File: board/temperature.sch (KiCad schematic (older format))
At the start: 3 parts, among them P201 CONN_2, U201 MAX6675

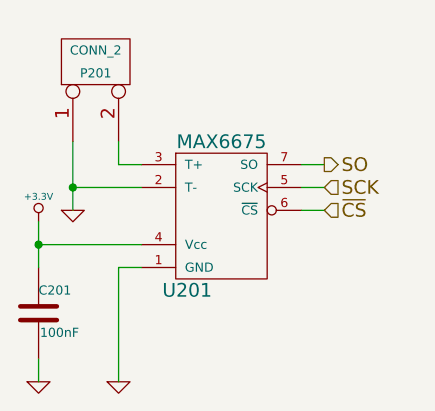
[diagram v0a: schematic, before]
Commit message: Selected Part Numbers for all Components
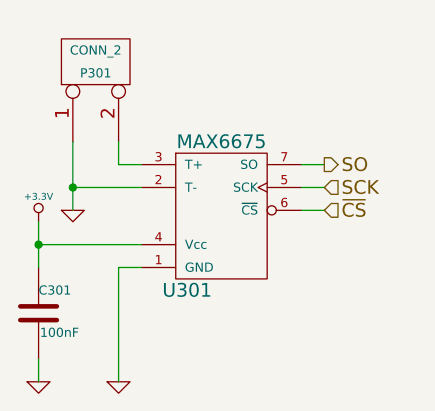
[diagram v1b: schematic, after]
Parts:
- C201: Part Number (none) -> CL10F104ZA8NNNC
- P201: Part Number (none) -> 1716020000
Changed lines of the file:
@@
 AR Path="/52EEE819/52E6B9FE" Ref="C201"  Part="1"
 AR Path="/52E79355/52E6B9FE" Ref="C301"  Part="1"
-F 0 "C201" H 4850 3900 40  0000 L CNN
+F 0 "C301" H 4850 3900 40  0000 L CNN
 F 1 "100nF" H 4856 3715 40  0000 L CNN
 F 2 "" H 4888 3650 30  0000 C CNN
 F 3 "" H 4850 3800 60  0000 C CNN
+F 4 "CL10F104ZA8NNNC" H 4850 3800 60  0001 C CNN "Part Number"
 	1    4850 3800
 	1    0    0    -1
 $EndComp
 $Comp
-L GND #PWR0116
+L GND #PWR0121
 U 1 1 52E6BA13
 P 5200 4100
-AR Path="/52EEE819/52E6BA13" Ref="#PWR0116"  Part="1"
-AR Path="/52E79355/52E6BA13" Ref="#PWR0120"  Part="1"
-F 0 "#PWR0116" H 5200 4100 30  0001 C CNN
+AR Path="/52EEE819/52E6BA13" Ref="#PWR0121"  Part="1"
+AR Path="/52E79355/52E6BA13" Ref="#PWR0125"  Part="1"
+F 0 "#PWR0125" H 5200 4100 30  0001 C CNN
 F 1 "GND" H 5200 4030 30  0001 C CNN
 F 2 "" H 5200 4100 60  0000 C CNN
@@
 	4850 3400 4850 3600
 $Comp
-L +3.3V #PWR0117
+L +3.3V #PWR0122
 U 1 1 52E6BA4F
 P 4850 3400
-AR Path="/52EEE819/52E6BA4F" Ref="#PWR0117"  Part="1"
-AR Path="/52E79355/52E6BA4F" Ref="#PWR0121"  Part="1"
-F 0 "#PWR0117" H 4850 3360 30  0001 C CNN
+AR Path="/52EEE819/52E6BA4F" Ref="#PWR0122"  Part="1"
+AR Path="/52E79355/52E6BA4F" Ref="#PWR0126"  Part="1"
+F 0 "#PWR0126" H 4850 3360 30  0001 C CNN
 F 1 "+3.3V" H 4850 3510 30  0000 C CNN
 F 2 "" H 4850 3400 60  0000 C CNN
@@
 Connection ~ 4850 3500
 $Comp
-L GND #PWR0118
+L GND #PWR0123
 U 1 1 52E6BA82
 P 4850 4100
-AR Path="/52EEE819/52E6BA82" Ref="#PWR0118"  Part="1"
-AR Path="/52E79355/52E6BA82" Ref="#PWR0122"  Part="1"
-F 0 "#PWR0118" H 4850 4100 30  0001 C CNN
+AR Path="/52EEE819/52E6BA82" Ref="#PWR0123"  Part="1"
+AR Path="/52E79355/52E6BA82" Ref="#PWR0127"  Part="1"
+F 0 "#PWR0127" H 4850 4100 30  0001 C CNN
 F 1 "GND" H 4850 4030 30  0001 C CNN
 F 2 "" H 4850 4100 60  0000 C CNN
@@
 AR Path="/52EEE819/52E6BAA9" Ref="P201"  Part="1"
 AR Path="/52E79355/52E6BAA9" Ref="P301"  Part="1"
-F 0 "P201" V 5050 2700 40  0000 C CNN
+F 0 "P301" V 5050 2700 40  0000 C CNN
 F 1 "CONN_2" V 5150 2700 40  0000 C CNN
 F 2 "" H 5100 2700 60  0000 C CNN
 F 3 "" H 5100 2700 60  0000 C CNN
+F 4 "1716020000" V 5100 2700 60  0001 C CNN "Part Number"
 	1    5100 2700
 	0    -1   -1   0
@@
 AR Path="/52EEE819/52E6BBF9" Ref="U201"  Part="1"
 AR Path="/52E79355/52E6BBF9" Ref="U301"  Part="1"
-F 0 "U201" H 5500 3100 60  0000 C CNN
+F 0 "U301" H 5500 3100 60  0000 C CNN
 F 1 "MAX6675" H 5650 3750 60  0000 C CNN
 F 2 "" H 5650 3400 60  0000 C CNN
@@
 $EndComp
 $Comp
-L GND #PWR0119
+L GND #PWR0124
 U 1 1 52E6BC15
 P 5000 3350
-AR Path="/52EEE819/52E6BC15" Ref="#PWR0119"  Part="1"
-AR Path="/52E79355/52E6BC15" Ref="#PWR0123"  Part="1"
-F 0 "#PWR0119" H 5000 3350 30  0001 C CNN
+AR Path="/52EEE819/52E6BC15" Ref="#PWR0124"  Part="1"
+AR Path="/52E79355/52E6BC15" Ref="#PWR0128"  Part="1"
+F 0 "#PWR0128" H 5000 3350 30  0001 C CNN
 F 1 "GND" H 5000 3280 30  0001 C CNN
 F 2 "" H 5000 3350 60  0000 C CNN

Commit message: Resolved issues while associating footprints.
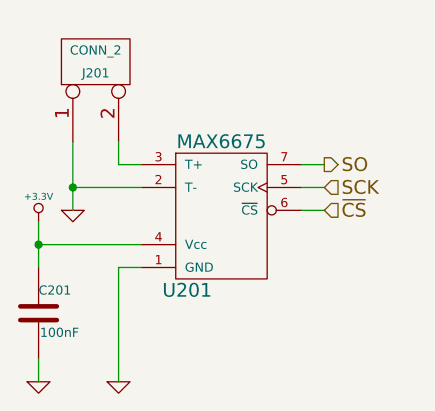
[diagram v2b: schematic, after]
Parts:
- renumbered P201 to J201
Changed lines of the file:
@@
 AR Path="/52EEE819/52E6B9FE" Ref="C201"  Part="1"
 AR Path="/52E79355/52E6B9FE" Ref="C301"  Part="1"
-F 0 "C301" H 4850 3900 40  0000 L CNN
+F 0 "C201" H 4850 3900 40  0000 L CNN
 F 1 "100nF" H 4856 3715 40  0000 L CNN
 F 2 "" H 4888 3650 30  0000 C CNN
@@
 $EndComp
 $Comp
-L GND #PWR0121
+L GND #PWR219
 U 1 1 52E6BA13
 P 5200 4100
-AR Path="/52EEE819/52E6BA13" Ref="#PWR0121"  Part="1"
-AR Path="/52E79355/52E6BA13" Ref="#PWR0125"  Part="1"
-F 0 "#PWR0125" H 5200 4100 30  0001 C CNN
+AR Path="/52EEE819/52E6BA13" Ref="#PWR219"  Part="1"
+AR Path="/52E79355/52E6BA13" Ref="#PWR304"  Part="1"
+F 0 "#PWR219" H 5200 4100 30  0001 C CNN
 F 1 "GND" H 5200 4030 30  0001 C CNN
 F 2 "" H 5200 4100 60  0000 C CNN
@@
 	4850 3400 4850 3600
 $Comp
-L +3.3V #PWR0122
+L +3.3V #PWR217
 U 1 1 52E6BA4F
 P 4850 3400
-AR Path="/52EEE819/52E6BA4F" Ref="#PWR0122"  Part="1"
-AR Path="/52E79355/52E6BA4F" Ref="#PWR0126"  Part="1"
-F 0 "#PWR0126" H 4850 3360 30  0001 C CNN
+AR Path="/52EEE819/52E6BA4F" Ref="#PWR217"  Part="1"
+AR Path="/52E79355/52E6BA4F" Ref="#PWR302"  Part="1"
+F 0 "#PWR217" H 4850 3360 30  0001 C CNN
 F 1 "+3.3V" H 4850 3510 30  0000 C CNN
 F 2 "" H 4850 3400 60  0000 C CNN
@@
 Connection ~ 4850 3500
 $Comp
-L GND #PWR0123
+L GND #PWR218
 U 1 1 52E6BA82
 P 4850 4100
-AR Path="/52EEE819/52E6BA82" Ref="#PWR0123"  Part="1"
-AR Path="/52E79355/52E6BA82" Ref="#PWR0127"  Part="1"
-F 0 "#PWR0127" H 4850 4100 30  0001 C CNN
+AR Path="/52EEE819/52E6BA82" Ref="#PWR218"  Part="1"
+AR Path="/52E79355/52E6BA82" Ref="#PWR303"  Part="1"
+F 0 "#PWR218" H 4850 4100 30  0001 C CNN
 F 1 "GND" H 4850 4030 30  0001 C CNN
 F 2 "" H 4850 4100 60  0000 C CNN
@@
 	4850 4000 4850 4100
 $Comp
-L CONN_2 P201
+L CONN_2 J201
 U 1 1 52E6BAA9
 P 5100 2700
-AR Path="/52EEE819/52E6BAA9" Ref="P201"  Part="1"
-AR Path="/52E79355/52E6BAA9" Ref="P301"  Part="1"
-F 0 "P301" V 5050 2700 40  0000 C CNN
+AR Path="/52EEE819/52E6BAA9" Ref="J201"  Part="1"
+AR Path="/52E79355/52E6BAA9" Ref="J301"  Part="1"
+F 0 "J201" V 5050 2700 40  0000 C CNN
 F 1 "CONN_2" V 5150 2700 40  0000 C CNN
 F 2 "" H 5100 2700 60  0000 C CNN
@@
 AR Path="/52EEE819/52E6BBF9" Ref="U201"  Part="1"
 AR Path="/52E79355/52E6BBF9" Ref="U301"  Part="1"
-F 0 "U301" H 5500 3100 60  0000 C CNN
+F 0 "U201" H 5500 3100 60  0000 C CNN
 F 1 "MAX6675" H 5650 3750 60  0000 C CNN
 F 2 "" H 5650 3400 60  0000 C CNN
@@
 $EndComp
 $Comp
-L GND #PWR0124
+L GND #PWR216
 U 1 1 52E6BC15
 P 5000 3350
-AR Path="/52EEE819/52E6BC15" Ref="#PWR0124"  Part="1"
-AR Path="/52E79355/52E6BC15" Ref="#PWR0128"  Part="1"
-F 0 "#PWR0128" H 5000 3350 30  0001 C CNN
+AR Path="/52EEE819/52E6BC15" Ref="#PWR216"  Part="1"
+AR Path="/52E79355/52E6BC15" Ref="#PWR301"  Part="1"
+F 0 "#PWR216" H 5000 3350 30  0001 C CNN
 F 1 "GND" H 5000 3280 30  0001 C CNN
 F 2 "" H 5000 3350 60  0000 C CNN

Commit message: Digikey Number + Link
Added a digikey part number and link to all components.
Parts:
- C201: Digikey Number (none) -> 1276-1011-1-ND; Part Number CL10F104ZA8NNNC -> (none)
- J201: Digikey Number (none) -> 281-1435-ND; Part Number 1716020000 -> (none)
- U201: Digikey Number (none) -> MAX6675ISA+TCT-ND; Part Number MAX6675 -> (none)
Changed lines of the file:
@@
 F 1 "100nF" H 4856 3715 40  0000 L CNN
 F 2 "" H 4888 3650 30  0000 C CNN
-F 3 "" H 4850 3800 60  0000 C CNN
-F 4 "CL10F104ZA8NNNC" H 4850 3800 60  0001 C CNN "Part Number"
+F 3 "http://www.digikey.ca/product-detail/en/CL10F104ZA8NNNC/1276-1011-1-ND/3889097" H 4850 3800 60  0001 C CNN
+F 4 "1276-1011-1-ND" H 6900 4550 60  0001 C CNN "Digikey Number"
 	1    4850 3800
 	1    0    0    -1
@@
 F 1 "CONN_2" V 5150 2700 40  0000 C CNN
 F 2 "" H 5100 2700 60  0000 C CNN
-F 3 "" H 5100 2700 60  0000 C CNN
-F 4 "1716020000" V 5100 2700 60  0001 C CNN "Part Number"
+F 3 "http://www.digikey.ca/product-search/en?vendor=0&keywords=1716020000" H 5100 2700 60  0001 C CNN
+F 4 "281-1435-ND" H 6900 4550 60  0001 C CNN "Digikey Number"
 	1    5100 2700
 	0    -1   -1   0
@@
 F 1 "MAX6675" H 5650 3750 60  0000 C CNN
 F 2 "" H 5650 3400 60  0000 C CNN
-F 3 "" H 5650 3400 60  0000 C CNN
-F 4 "MAX6675" H 5650 3400 60  0001 C CNN "Part Number"
+F 3 "http://www.digikey.ca/product-detail/en/MAX6675ISA%2BT/MAX6675ISA%2BTCT-ND/1859231" H 5650 3400 60  0001 C CNN
+F 4 "MAX6675ISA+TCT-ND" H 6900 4550 60  0001 C CNN "Digikey Number"
 	1    5650 3400
 	1    0    0    -1

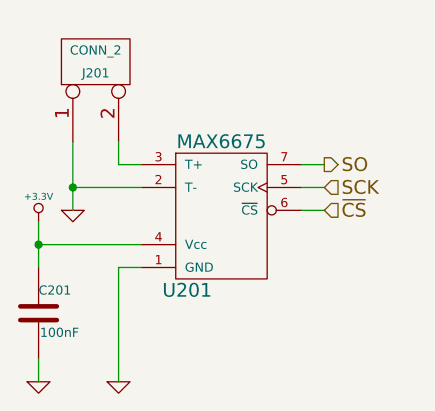
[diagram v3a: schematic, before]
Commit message: Prepared components/footprints for PCB Layout.
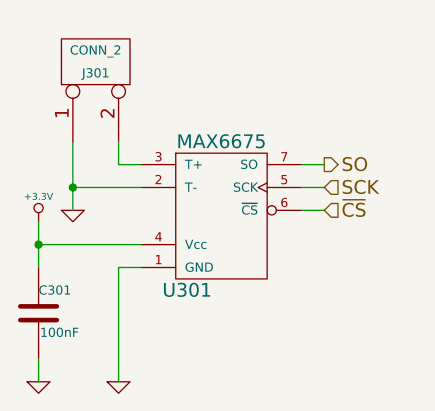
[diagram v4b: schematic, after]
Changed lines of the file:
@@
 AR Path="/52EEE819/52E6B9FE" Ref="C201"  Part="1"
 AR Path="/52E79355/52E6B9FE" Ref="C301"  Part="1"
-F 0 "C201" H 4850 3900 40  0000 L CNN
+F 0 "C301" H 4850 3900 40  0000 L CNN
 F 1 "100nF" H 4856 3715 40  0000 L CNN
 F 2 "" H 4888 3650 30  0000 C CNN
@@
 $EndComp
 $Comp
-L GND #PWR219
+L GND #PWR0121
 U 1 1 52E6BA13
 P 5200 4100
-AR Path="/52EEE819/52E6BA13" Ref="#PWR219"  Part="1"
-AR Path="/52E79355/52E6BA13" Ref="#PWR304"  Part="1"
-F 0 "#PWR219" H 5200 4100 30  0001 C CNN
+AR Path="/52EEE819/52E6BA13" Ref="#PWR0121"  Part="1"
+AR Path="/52E79355/52E6BA13" Ref="#PWR0125"  Part="1"
+F 0 "#PWR0125" H 5200 4100 30  0001 C CNN
 F 1 "GND" H 5200 4030 30  0001 C CNN
 F 2 "" H 5200 4100 60  0000 C CNN
@@
 	4850 3400 4850 3600
 $Comp
-L +3.3V #PWR217
+L +3.3V #PWR0122
 U 1 1 52E6BA4F
 P 4850 3400
-AR Path="/52EEE819/52E6BA4F" Ref="#PWR217"  Part="1"
-AR Path="/52E79355/52E6BA4F" Ref="#PWR302"  Part="1"
-F 0 "#PWR217" H 4850 3360 30  0001 C CNN
+AR Path="/52EEE819/52E6BA4F" Ref="#PWR0122"  Part="1"
+AR Path="/52E79355/52E6BA4F" Ref="#PWR0126"  Part="1"
+F 0 "#PWR0126" H 4850 3360 30  0001 C CNN
 F 1 "+3.3V" H 4850 3510 30  0000 C CNN
 F 2 "" H 4850 3400 60  0000 C CNN
@@
 Connection ~ 4850 3500
 $Comp
-L GND #PWR218
+L GND #PWR0123
 U 1 1 52E6BA82
 P 4850 4100
-AR Path="/52EEE819/52E6BA82" Ref="#PWR218"  Part="1"
-AR Path="/52E79355/52E6BA82" Ref="#PWR303"  Part="1"
-F 0 "#PWR218" H 4850 4100 30  0001 C CNN
+AR Path="/52EEE819/52E6BA82" Ref="#PWR0123"  Part="1"
+AR Path="/52E79355/52E6BA82" Ref="#PWR0127"  Part="1"
+F 0 "#PWR0127" H 4850 4100 30  0001 C CNN
 F 1 "GND" H 4850 4030 30  0001 C CNN
 F 2 "" H 4850 4100 60  0000 C CNN
@@
 AR Path="/52EEE819/52E6BAA9" Ref="J201"  Part="1"
 AR Path="/52E79355/52E6BAA9" Ref="J301"  Part="1"
-F 0 "J201" V 5050 2700 40  0000 C CNN
+F 0 "J301" V 5050 2700 40  0000 C CNN
 F 1 "CONN_2" V 5150 2700 40  0000 C CNN
 F 2 "" H 5100 2700 60  0000 C CNN
@@
 AR Path="/52EEE819/52E6BBF9" Ref="U201"  Part="1"
 AR Path="/52E79355/52E6BBF9" Ref="U301"  Part="1"
-F 0 "U201" H 5500 3100 60  0000 C CNN
+F 0 "U301" H 5500 3100 60  0000 C CNN
 F 1 "MAX6675" H 5650 3750 60  0000 C CNN
 F 2 "" H 5650 3400 60  0000 C CNN
@@
 $EndComp
 $Comp
-L GND #PWR216
+L GND #PWR0124
 U 1 1 52E6BC15
 P 5000 3350
-AR Path="/52EEE819/52E6BC15" Ref="#PWR216"  Part="1"
-AR Path="/52E79355/52E6BC15" Ref="#PWR301"  Part="1"
-F 0 "#PWR216" H 5000 3350 30  0001 C CNN
+AR Path="/52EEE819/52E6BC15" Ref="#PWR0124"  Part="1"
+AR Path="/52E79355/52E6BC15" Ref="#PWR0128"  Part="1"
+F 0 "#PWR0128" H 5000 3350 30  0001 C CNN
 F 1 "GND" H 5000 3280 30  0001 C CNN
 F 2 "" H 5000 3350 60  0000 C CNN

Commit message: Made use of new components
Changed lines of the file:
@@
 AR Path="/52EEE819/52E6B9FE" Ref="C201"  Part="1"
 AR Path="/52E79355/52E6B9FE" Ref="C301"  Part="1"
-F 0 "C301" H 4850 3900 40  0000 L CNN
+F 0 "C201" H 4850 3900 40  0000 L CNN
 F 1 "100nF" H 4856 3715 40  0000 L CNN
 F 2 "" H 4888 3650 30  0000 C CNN
@@
 AR Path="/52EEE819/52E6BA13" Ref="#PWR0120"  Part="1"
 AR Path="/52E79355/52E6BA13" Ref="#PWR0124"  Part="1"
-F 0 "#PWR0124" H 5200 4100 30  0001 C CNN
+F 0 "#PWR0120" H 5200 4100 30  0001 C CNN
 F 1 "GND" H 5200 4030 30  0001 C CNN
 F 2 "" H 5200 4100 60  0000 C CNN
@@
 AR Path="/52EEE819/52E6BA4F" Ref="#PWR0121"  Part="1"
 AR Path="/52E79355/52E6BA4F" Ref="#PWR0125"  Part="1"
-F 0 "#PWR0125" H 4850 3360 30  0001 C CNN
+F 0 "#PWR0121" H 4850 3360 30  0001 C CNN
 F 1 "+3.3V" H 4850 3510 30  0000 C CNN
 F 2 "" H 4850 3400 60  0000 C CNN
@@
 AR Path="/52EEE819/52E6BA82" Ref="#PWR0122"  Part="1"
 AR Path="/52E79355/52E6BA82" Ref="#PWR0126"  Part="1"
-F 0 "#PWR0126" H 4850 4100 30  0001 C CNN
+F 0 "#PWR0122" H 4850 4100 30  0001 C CNN
 F 1 "GND" H 4850 4030 30  0001 C CNN
 F 2 "" H 4850 4100 60  0000 C CNN
@@
 AR Path="/52EEE819/52E6BAA9" Ref="J201"  Part="1"
 AR Path="/52E79355/52E6BAA9" Ref="J301"  Part="1"
-F 0 "J301" V 5050 2700 40  0000 C CNN
+F 0 "J201" V 5050 2700 40  0000 C CNN
 F 1 "CONN_2" V 5150 2700 40  0000 C CNN
 F 2 "" H 5100 2700 60  0000 C CNN
@@
 AR Path="/52EEE819/52E6BBF9" Ref="U201"  Part="1"
 AR Path="/52E79355/52E6BBF9" Ref="U301"  Part="1"
-F 0 "U301" H 5500 3100 60  0000 C CNN
+F 0 "U201" H 5500 3100 60  0000 C CNN
 F 1 "MAX6675" H 5650 3750 60  0000 C CNN
 F 2 "" H 5650 3400 60  0000 C CNN
@@
 AR Path="/52EEE819/52E6BC15" Ref="#PWR0123"  Part="1"
 AR Path="/52E79355/52E6BC15" Ref="#PWR0127"  Part="1"
-F 0 "#PWR0127" H 5000 3350 30  0001 C CNN
+F 0 "#PWR0123" H 5000 3350 30  0001 C CNN
 F 1 "GND" H 5000 3280 30  0001 C CNN
 F 2 "" H 5000 3350 60  0000 C CNN

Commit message: Layed out in general where stuff is going to be located.
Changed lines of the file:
@@
 AR Path="/52EEE819/52E6B9FE" Ref="C201"  Part="1"
 AR Path="/52E79355/52E6B9FE" Ref="C301"  Part="1"
-F 0 "C201" H 4850 3900 40  0000 L CNN
+F 0 "C301" H 4850 3900 40  0000 L CNN
 F 1 "100nF" H 4856 3715 40  0000 L CNN
 F 2 "" H 4888 3650 30  0000 C CNN
@@
 $EndComp
 $Comp
-L GND #PWR0120
+L GND #PWR218
 U 1 1 52E6BA13
 P 5200 4100
-AR Path="/52EEE819/52E6BA13" Ref="#PWR0120"  Part="1"
-AR Path="/52E79355/52E6BA13" Ref="#PWR0124"  Part="1"
-F 0 "#PWR0120" H 5200 4100 30  0001 C CNN
+AR Path="/52EEE819/52E6BA13" Ref="#PWR218"  Part="1"
+AR Path="/52E79355/52E6BA13" Ref="#PWR304"  Part="1"
+F 0 "#PWR304" H 5200 4100 30  0001 C CNN
 F 1 "GND" H 5200 4030 30  0001 C CNN
 F 2 "" H 5200 4100 60  0000 C CNN
@@
 	4850 3400 4850 3600
 $Comp
-L +3.3V #PWR0121
+L +3.3V #PWR216
 U 1 1 52E6BA4F
 P 4850 3400
-AR Path="/52EEE819/52E6BA4F" Ref="#PWR0121"  Part="1"
-AR Path="/52E79355/52E6BA4F" Ref="#PWR0125"  Part="1"
-F 0 "#PWR0121" H 4850 3360 30  0001 C CNN
+AR Path="/52EEE819/52E6BA4F" Ref="#PWR216"  Part="1"
+AR Path="/52E79355/52E6BA4F" Ref="#PWR302"  Part="1"
+F 0 "#PWR302" H 4850 3360 30  0001 C CNN
 F 1 "+3.3V" H 4850 3510 30  0000 C CNN
 F 2 "" H 4850 3400 60  0000 C CNN
@@
 Connection ~ 4850 3500
 $Comp
-L GND #PWR0122
+L GND #PWR217
 U 1 1 52E6BA82
 P 4850 4100
-AR Path="/52EEE819/52E6BA82" Ref="#PWR0122"  Part="1"
-AR Path="/52E79355/52E6BA82" Ref="#PWR0126"  Part="1"
-F 0 "#PWR0122" H 4850 4100 30  0001 C CNN
+AR Path="/52EEE819/52E6BA82" Ref="#PWR217"  Part="1"
+AR Path="/52E79355/52E6BA82" Ref="#PWR303"  Part="1"
+F 0 "#PWR303" H 4850 4100 30  0001 C CNN
 F 1 "GND" H 4850 4030 30  0001 C CNN
 F 2 "" H 4850 4100 60  0000 C CNN
@@
 AR Path="/52EEE819/52E6BAA9" Ref="J201"  Part="1"
 AR Path="/52E79355/52E6BAA9" Ref="J301"  Part="1"
-F 0 "J201" V 5050 2700 40  0000 C CNN
+F 0 "J301" V 5050 2700 40  0000 C CNN
 F 1 "CONN_2" V 5150 2700 40  0000 C CNN
 F 2 "" H 5100 2700 60  0000 C CNN
@@
 AR Path="/52EEE819/52E6BBF9" Ref="U201"  Part="1"
 AR Path="/52E79355/52E6BBF9" Ref="U301"  Part="1"
-F 0 "U201" H 5500 3100 60  0000 C CNN
+F 0 "U301" H 5500 3100 60  0000 C CNN
 F 1 "MAX6675" H 5650 3750 60  0000 C CNN
 F 2 "" H 5650 3400 60  0000 C CNN
@@
 $EndComp
 $Comp
-L GND #PWR0123
+L GND #PWR215
 U 1 1 52E6BC15
 P 5000 3350
-AR Path="/52EEE819/52E6BC15" Ref="#PWR0123"  Part="1"
-AR Path="/52E79355/52E6BC15" Ref="#PWR0127"  Part="1"
-F 0 "#PWR0123" H 5000 3350 30  0001 C CNN
+AR Path="/52EEE819/52E6BC15" Ref="#PWR215"  Part="1"
+AR Path="/52E79355/52E6BC15" Ref="#PWR301"  Part="1"
+F 0 "#PWR301" H 5000 3350 30  0001 C CNN
 F 1 "GND" H 5000 3280 30  0001 C CNN
 F 2 "" H 5000 3350 60  0000 C CNN

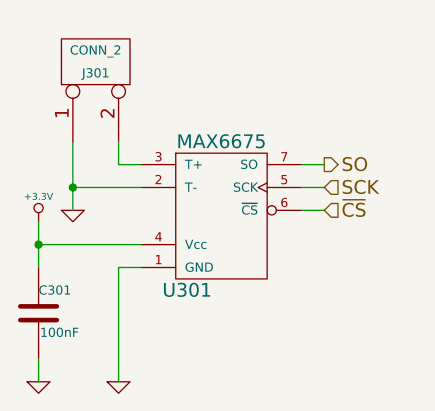
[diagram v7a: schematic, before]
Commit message: Named all connectors/leds/switches based on their functionality, refdes's are safe.
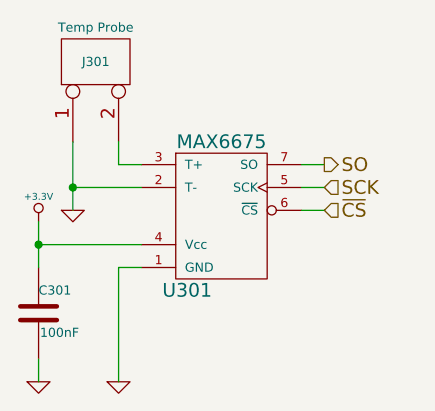
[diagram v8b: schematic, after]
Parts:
- J201: value CONN_2 -> Temp Probe
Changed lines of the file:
@@
 $Descr A4 11693 8268
 encoding utf-8
-Sheet 2 26
+Sheet 3 26
 Title "K-Type Temperature Sensor"
 Date ""
@@
 $EndComp
 $Comp
-L GND #PWR218
+L GND #PWR0120
 U 1 1 52E6BA13
 P 5200 4100
-AR Path="/52EEE819/52E6BA13" Ref="#PWR218"  Part="1"
-AR Path="/52E79355/52E6BA13" Ref="#PWR304"  Part="1"
-F 0 "#PWR304" H 5200 4100 30  0001 C CNN
+AR Path="/52EEE819/52E6BA13" Ref="#PWR0120"  Part="1"
+AR Path="/52E79355/52E6BA13" Ref="#PWR0124"  Part="1"
+F 0 "#PWR0124" H 5200 4100 30  0001 C CNN
 F 1 "GND" H 5200 4030 30  0001 C CNN
 F 2 "" H 5200 4100 60  0000 C CNN
@@
 	4850 3400 4850 3600
 $Comp
-L +3.3V #PWR216
+L +3.3V #PWR0121
 U 1 1 52E6BA4F
 P 4850 3400
-AR Path="/52EEE819/52E6BA4F" Ref="#PWR216"  Part="1"
-AR Path="/52E79355/52E6BA4F" Ref="#PWR302"  Part="1"
-F 0 "#PWR302" H 4850 3360 30  0001 C CNN
+AR Path="/52EEE819/52E6BA4F" Ref="#PWR0121"  Part="1"
+AR Path="/52E79355/52E6BA4F" Ref="#PWR0125"  Part="1"
+F 0 "#PWR0125" H 4850 3360 30  0001 C CNN
 F 1 "+3.3V" H 4850 3510 30  0000 C CNN
 F 2 "" H 4850 3400 60  0000 C CNN
@@
 Connection ~ 4850 3500
 $Comp
-L GND #PWR217
+L GND #PWR0122
 U 1 1 52E6BA82
 P 4850 4100
-AR Path="/52EEE819/52E6BA82" Ref="#PWR217"  Part="1"
-AR Path="/52E79355/52E6BA82" Ref="#PWR303"  Part="1"
-F 0 "#PWR303" H 4850 4100 30  0001 C CNN
+AR Path="/52EEE819/52E6BA82" Ref="#PWR0122"  Part="1"
+AR Path="/52E79355/52E6BA82" Ref="#PWR0126"  Part="1"
+F 0 "#PWR0126" H 4850 4100 30  0001 C CNN
 F 1 "GND" H 4850 4030 30  0001 C CNN
 F 2 "" H 4850 4100 60  0000 C CNN
@@
 AR Path="/52EEE819/52E6BAA9" Ref="J201"  Part="1"
 AR Path="/52E79355/52E6BAA9" Ref="J301"  Part="1"
-F 0 "J301" V 5050 2700 40  0000 C CNN
-F 1 "CONN_2" V 5150 2700 40  0000 C CNN
+F 0 "J301" V 5100 2700 40  0000 C CNN
+F 1 "Temp Probe" V 5250 2700 40  0000 C CNN
 F 2 "" H 5100 2700 60  0000 C CNN
 F 3 "http://www.digikey.ca/product-search/en?vendor=0&keywords=1716020000" H 5100 2700 60  0001 C CNN
@@
 $EndComp
 $Comp
-L GND #PWR215
+L GND #PWR0123
 U 1 1 52E6BC15
 P 5000 3350
-AR Path="/52EEE819/52E6BC15" Ref="#PWR215"  Part="1"
-AR Path="/52E79355/52E6BC15" Ref="#PWR301"  Part="1"
-F 0 "#PWR301" H 5000 3350 30  0001 C CNN
+AR Path="/52EEE819/52E6BC15" Ref="#PWR0123"  Part="1"
+AR Path="/52E79355/52E6BC15" Ref="#PWR0127"  Part="1"
+F 0 "#PWR0127" H 5000 3350 30  0001 C CNN
 F 1 "GND" H 5000 3280 30  0001 C CNN
 F 2 "" H 5000 3350 60  0000 C CNN
